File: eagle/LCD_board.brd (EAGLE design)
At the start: 160 x 100 mm, 5 parts, among them CN1 1X4-CLEANBIG

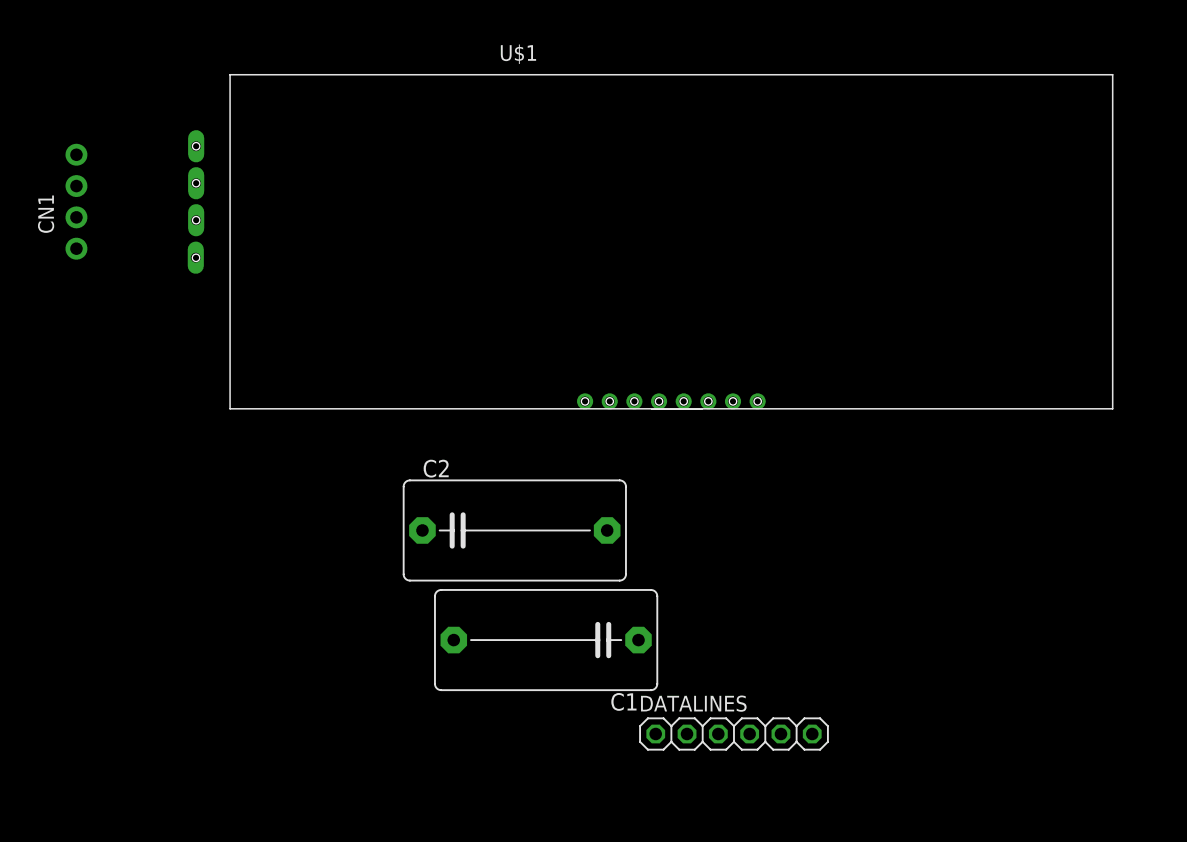
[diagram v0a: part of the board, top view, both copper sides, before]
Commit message: Routed wires for the LCD_board.brd file. Most of the errors were removed when running DRC with the EPL design rules supplied from git.  Also removed the drills fron the LDC sceen footprint.  When placing a pad there is a drill already associated with it, adding another drill is redundant and not needed.
There is still an error on the LDC_board.brd which seems to be related to the 8pins and the outline of the LDC sceen. I think these can be ignored but I need to check on these.
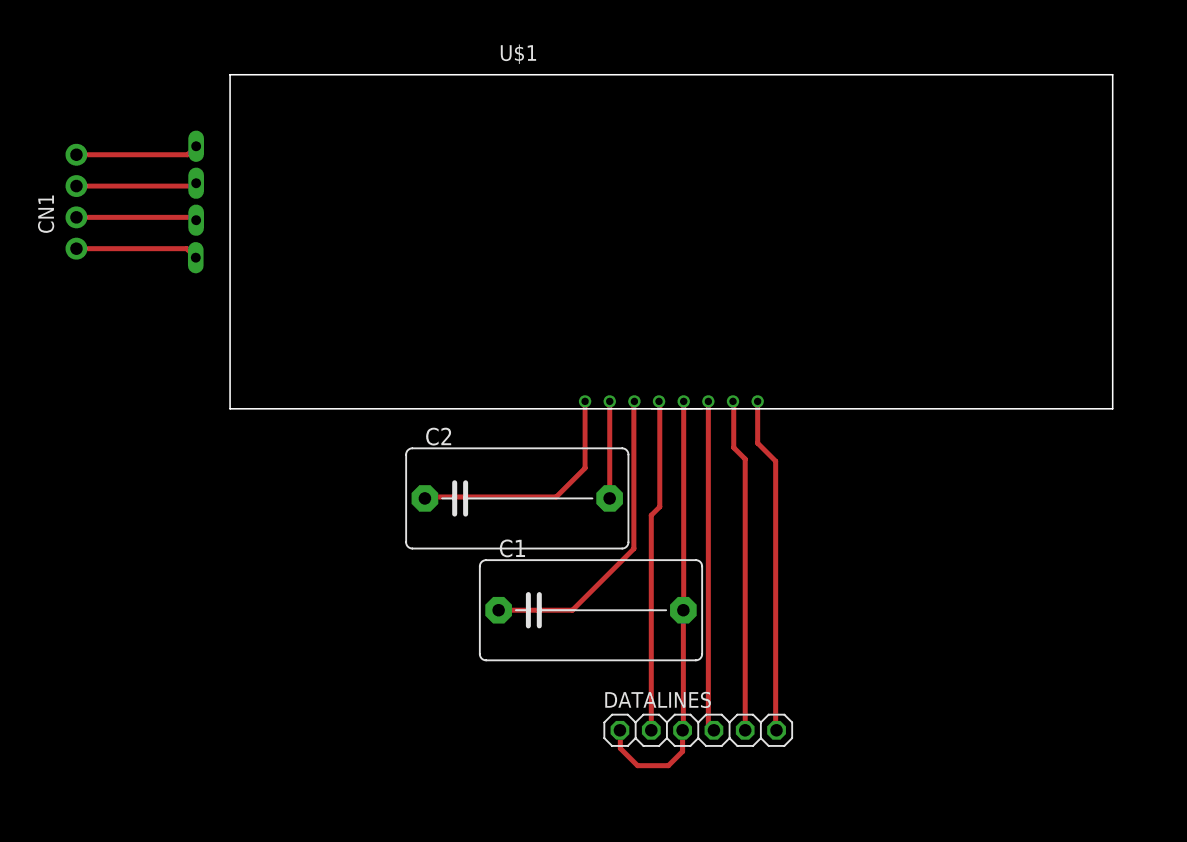
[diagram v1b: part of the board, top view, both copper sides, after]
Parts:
- moved C1 4.37 mm to (72.2, 36.7), turned to 0 degrees
- moved DATALINES 2.92 mm to (80.9, 27.0)
- moved C2 2.61 mm to (66.2, 45.8)
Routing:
- net GND: track 0.00 -> 36.0 mm
- net RST: track 0.00 -> 27.3 mm
- net SCL: track 0.00 -> 27.1 mm
- net VDD: track 0.00 -> 27.0 mm
- net SDA: track 0.00 -> 26.9 mm
- net N$3: track 0.00 -> 25.0 mm
- net N$1: track 0.00 -> 19.4 mm
- net A: track 0.00 -> 10.00 mm
- net N$4: track 0.00 -> 9.98 mm
- net GK: track 0.00 -> 9.81 mm
- net N$2: track 0.00 -> 9.81 mm
- net C1+: track 0.00 -> 7.87 mm
